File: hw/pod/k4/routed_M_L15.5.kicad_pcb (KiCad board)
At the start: 6 copper layers, 15.5 x 12 mm, 32 parts, among them J10 TestPoint_Pad_D1.0mm, J11 TestPoint_Pad_D1.0mm, J20 CONN-SMD_BM28B0.6-30DS-2-0.35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, J3 TestPoint_Pad_D1.0mm, J4 WirePad_1.0x2.0mm, J5 TestPoint_Pad_D1.0mm, J7 TestPoint_Pad_D1.0mm, J8 TestPoint_Pad_D1.0mm, J9 TestPoint_Pad_D1.0mm, SW1 SW-SMD_4P-L3.0-W2.6-P1.85-LS3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, U2 Knowles_LGA-5_3.5x2.65mm, U3 DSBGA-8_L1.6-W0.9-R2-C4-P0.40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, U4 X2SON-4_L1.0-W1.0-P0.65-TL-EP, U6 SOT-553-5_L1.6-W1.2-P0.50-LS1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

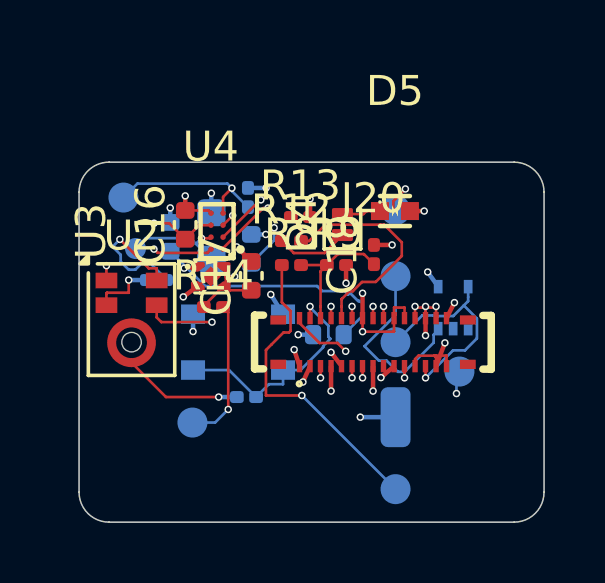
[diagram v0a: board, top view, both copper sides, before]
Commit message: K4 closure at L15.5: 5-part unload P->M + BM28 pins 26/27 swap (ECR-0020 rev 4); M and P both 0 open / 0 DRC / place PASS
Co-Authored-By: Claude Opus 5.5 <noreply@anthropic.com>
Claude-Session: https://claude.ai/code/session_01Wg997D6KFs8bxoAH56jZZJ
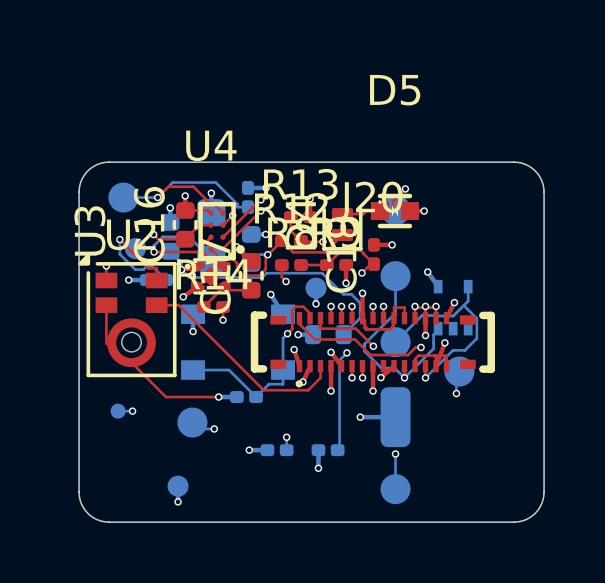
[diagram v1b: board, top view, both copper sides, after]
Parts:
- added R15: R_0201_0603Metric, R_0201_0603Metric, B.Cu at (6.60, 9.60)
- added R16: R_0201_0603Metric, R_0201_0603Metric, B.Cu at (8.30, 9.60)
- added TP10: TestDot_D0.5mm, TestDot_D0.5mm, B.Cu at (1.30, 8.30)
- added TP4: TestPoint_Pad_D0.7mm, TestPoint_Pad_D0.7mm, B.Cu at (7.90, 4.20)
- added TP5: TestPoint_Pad_D0.7mm, TestPoint_Pad_D0.7mm, B.Cu at (3.30, 10.8)
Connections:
- J20 pad 26: VBUS_SENSE -> CHG_INT
- J20 pad 27: CHG_INT -> VBUS_SENSE
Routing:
- net I2C_SCL: track 7.65 -> 15.6 mm, vias 2 -> 3
- net I2C_SDA: track 6.85 -> 12.0 mm, vias 2 -> 3
- net VBUS: track 10.9 -> 6.69 mm, vias 2 -> 1
- net VBUS_SENSE: track 8.47 -> 4.34 mm, vias 0 -> 2
- net VBAT: track 20.7 -> 16.6 mm, vias 2 -> 3
- net VBAT_SENSE: track 4.58 -> 8.52 mm, vias 0 -> 2
- net TS: track 13.1 -> 17.0 mm
- net MIC_DATA: track 11.3 -> 15.0 mm, vias 2 -> 3
- net +3V0: track 4.53 -> 6.27 mm, vias 7 -> 10
- net VSYS: track 7.49 -> 8.98 mm, vias 2 -> 1
- net GND: track 26.9 -> 28.0 mm
- net BTN: track 7.82 -> 7.04 mm
- net CHG_INT: track 6.62 -> 7.33 mm
- net MIC_VDD: track 15.2 -> 14.5 mm
- net LED_A: track 4.86 -> 5.14 mm, vias 1 -> 2
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
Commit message: K4 re-place/route after 9ec84ae: P and M at L 15.5, plain kicad-cli DRC 0 errors / 0 unconnected both; route_net3d GRID env; pin-contract + ECR-0020 + backlog (C9/C17 datasheet check still open)
Co-Authored-By: Claude Opus 5.5 <noreply@anthropic.com>
Claude-Session: https://claude.ai/code/session_01Wg997D6KFs8bxoAH56jZZJ
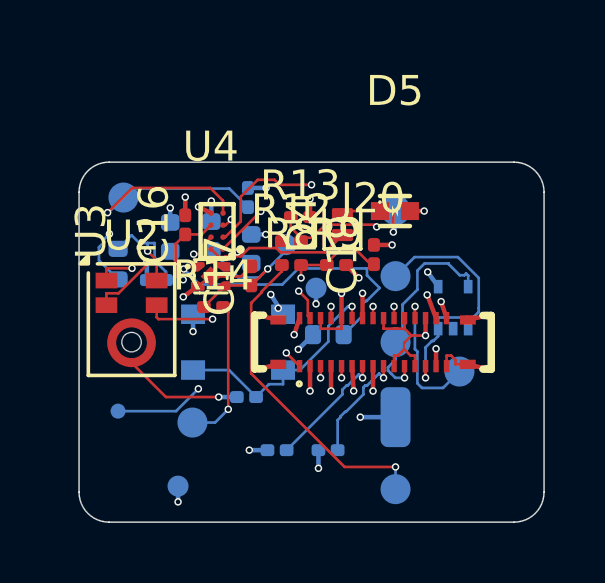
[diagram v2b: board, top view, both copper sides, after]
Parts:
- added R30: R_0402_1005Metric, R_0402_1005Metric, B.Cu at (1.30, 3.40)
- C16, C17: value C_0402_1005Metric -> C_0201_0603Metric; footprint C_0402_1005Metric -> C_0201_0603Metric
- C21: value C_0603_1608Metric -> C_0402_1005Metric; footprint C_0603_1608Metric -> C_0402_1005Metric
- moved TP6 5.02 mm to (6.90, 2.75)
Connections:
- C13 pad 1: MIC_VDD -> MIC_VDDF
- J20 pad 1: GND -> MIC_VDD
- J20 pad 11: USB_DP -> USB_DM
- J20 pad 13: USB_DM -> USB_DP
- J20 pad 15: GND -> +3V0
- J20 pad 17: +3V0 -> GND
- J20 pad 18: +3V0 -> GND
- J20 pad 19: +3V0 -> LED_K
- J20 pad 21: GND -> MIC_DATA
- J20 pad 22: TS -> GND
- J20 pad 23: I2C_SCL -> CHG_INT
- J20 pad 25: I2C_SDA -> BTN
- J20 pad 26: CHG_INT -> GND
- J20 pad 28: VBAT_SENSE -> GND
- J20 pad 29: BTN -> TS
- J20 pad 30: LED_K -> +3V0
- J20 pad 31: (no net) -> +3V0
- J20 pad 32: (no net) -> +3V0
- J20 pad 33: (no net) -> +3V0
- J20 pad 34: (no net) -> +3V0
- J20 pad 5: GND -> VBAT_SENSE
- J20 pad 6: MIC_VDD -> GND
- J20 pad 7: MIC_DATA -> I2C_SCL
- J20 pad 9: GND -> I2C_SDA
- U2 pad 5: MIC_VDD -> MIC_VDDF
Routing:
- net VBAT: track 16.6 -> 23.4 mm, vias 3 -> 2
- net MIC_VDD: track 14.5 -> 10.1 mm
- net MIC_VDDF: track 0.00 -> 4.28 mm, vias 0 -> 1
- net MIC_DATA: track 15.0 -> 19.1 mm
- net VBUS_SENSE: track 4.34 -> 7.39 mm
- net LED_K: track 7.58 -> 4.68 mm, vias 2 -> 1
- net GND: track 28.0 -> 30.7 mm, vias 25 -> 26
- net I2C_SCL: track 15.6 -> 17.6 mm, vias 3 -> 2
- net +3V0: track 6.27 -> 8.19 mm, vias 10 -> 12
- net TS: track 17.0 -> 18.6 mm
- net LDO_OUT: track 9.17 -> 10.7 mm
- net USB_DP: track 7.17 -> 8.49 mm
- net I2C_SDA: track 12.0 -> 13.1 mm, vias 3 -> 2
- net VBAT_SENSE: track 8.52 -> 7.66 mm
- net BTN: track 7.04 -> 7.89 mm
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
